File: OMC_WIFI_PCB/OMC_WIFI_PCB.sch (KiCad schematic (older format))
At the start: 27 parts, among them J1 SW, J10 Conn_01x02_Female_CanBus, J11 RJ14, J2 UART, J3 Screw_Terminal_01x02, J4 ICSP, J5 Conn_01x03_Female_SI, J6 Conn_01x02_Female_SV, J7 Conn_01x04_Female_SV, J8 Conn_01x03_Female_Rele, J9 Conn_01x07_Female_CanBus, SW1 SW_DIP_x06, U1 ATmega328P-MU, Y1 Crystal

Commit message: Actualización Esquemático
+ Módulo ZMPT101B
+ Módulo ACS712
+ ESP32 DevKitv1
+ Fuente de alimentación
+ Módulo Relay
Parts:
- removed C1: 0.1uf, SLAVE:CP_Radial_D5.0mm_P2.50mm, symbol Device:CP
- removed C2, C3: 22pF, SLAVE:C_0603_1608Metric_Pad1.05x0.95mm_HandSolder, symbol Device:C
- removed D1: LED, SLAVE:LED_D3.0mm, symbol Device:LED
- removed J1: SW, SLAVE:SolderWire-0.75sqmm_1x02_P4.8mm_D1.25mm_OD2.3mm, symbol Connector:Conn_01x02_Male
- removed J10: Conn_01x02_Female_CanBus, SLAVE:PinHeader_1x02_P2.54mm_Vertical, symbol Connector:Conn_01x02_Female
- removed J11: RJ14, SLAVE:RJ14_Connfly_DS1133-S4_Horizontal, symbol Connector:RJ13
- removed J2: UART, SLAVE:PinHeader_1x02_P2.54mm_Vertical, symbol Connector:Conn_01x02_Male
- removed J3: Screw_Terminal_01x02, SLAVE:TerminalBlock_bornier-2_P5.08mm, symbol Connector:Screw_Terminal_01x02
- removed J4: ICSP, SLAVE:PinHeader_2x03_P2.54mm_Vertical, symbol Connector_Generic:Conn_02x03_Odd_Even
- removed J6: Conn_01x02_Female_SV, SLAVE:SolderWire-0.75sqmm_1x02_P4.8mm_D1.25mm_OD2.3mm, symbol Connector:Conn_01x02_Female
- removed J7: Conn_01x04_Female_SV, SLAVE:PinHeader_1x04_P2.54mm_Vertical, symbol Connector:Conn_01x04_Female
- removed J8: Conn_01x03_Female_Rele, SLAVE:PinHeader_1x03_P2.54mm_Vertical, symbol Connector:Conn_01x03_Female
- removed J9: Conn_01x07_Female_CanBus, SLAVE:PinHeader_1x07_P2.54mm_Vertical, symbol Connector:Conn_01x07_Female
- removed PS1: HLK-PM01/5M05, SLAVE:Converter_ACDC_HiLink_HLK-PMxx, symbol Converter_ACDC:HLK-PM01
- removed R1, R3, R4, R5, R6, R7, R8: 10k, SLAVE:R_0603_1608Metric_Pad1.05x0.95mm_HandSolder, symbol Device:R
- removed R2: 330, SLAVE:R_0603_1608Metric_Pad1.05x0.95mm_HandSolder, symbol Device:R
- removed SW1: SW_DIP_x06, SLAVE:SW_DIP_SPSTx06_Piano_10.8x16.8mm_W7.62mm_P2.54mm, symbol Switch:SW_DIP_x06
- removed U1: ATmega328P-MU, SLAVE:TQFP-32_7x7mm_P0.8mm, symbol MCU_Microchip_ATmega:ATmega328P-MU
- removed Y1: Crystal, SLAVE:Crystal_SMD_HC49-SD, symbol Device:Crystal
- added J?: ESP32_Left, Connector_PinSocket_2.54mm:PinSocket_1x15_P2.54mm_Vertical, symbol Connector:Conn_01x15_Female
- added J?: ESP32_Right, Connector_PinSocket_2.54mm:PinSocket_1x15_P2.54mm_Vertical, symbol Connector:Conn_01x15_Female
- added J?: Conn_01x02_Female_SV, SLAVE:SolderWire-0.75sqmm_1x02_P4.8mm_D1.25mm_OD2.3mm, symbol Connector:Conn_01x02_Female
- added J?: Conn_01x02_Female, symbol Connector:Conn_01x02_Female
- added J?: Conn_01x04_Female, symbol Connector:Conn_01x04_Female
- added J?: Switch, Connector_PinHeader_2.54mm:PinHeader_1x02_P2.54mm_Vertical, symbol Connector:Conn_01x02_Male
- added J?: Conn_01x06_Female, symbol Connector:Conn_01x06_Female
- added J? (x2): Conn_01x03_Female, symbol Connector:Conn_01x03_Female
- added J?: Screw_Terminal_01x03, symbol Connector:Screw_Terminal_01x03
- added PS?: HLK-PM01, Converter_ACDC:Converter_ACDC_HiLink_HLK-PMxx, symbol Converter_ACDC:HLK-PM01
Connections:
- net labels added: 3V3, COM, CTS, D12, D13, D14, D15, D18, D19, D2, D21, D22, D23, D25, D26, D27_LED, D32_RELAY, D33, D34, D35, D4, D5, DTR, EN, I_ACS, NC, NO, RX0, RX2, TX0, TX2, VCC, VN_ACS, VP_ZMPT
- net labels removed: CS, H, INTERRUPT, I_Sensor, L, MISO, MOSI, RELAY, RESET, RX, SCK, TX, V_Sensor, XTAL1, XTAL2
- wire segments 144 -> 74
- no-connect marks 8 -> 1
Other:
- note added: "FT232R"
- note added: "Fuente de Alimentación HLK-PM01"
- note added: "Módulo ACS712 (Sensor Corriente)\n"
- note added: "Módulo ESP-WROOM32-DevKit1\n"
- note added: "Módulo Relay\n"
- note added: "Módulo ZMPT101B (Sensor Voltaje)\n"
- note removed: "Modulo CANBus con conector RJ11\n"
- note removed: "Modulo Relé\n"
- note removed: "Modulo Sensor Corriente\n"
- note removed: "Modulo Sensor Voltaje\n"
- note removed: "Programación ICSP\n"
- note removed: "Salida Serial\n"
- moved on the sheet: J5

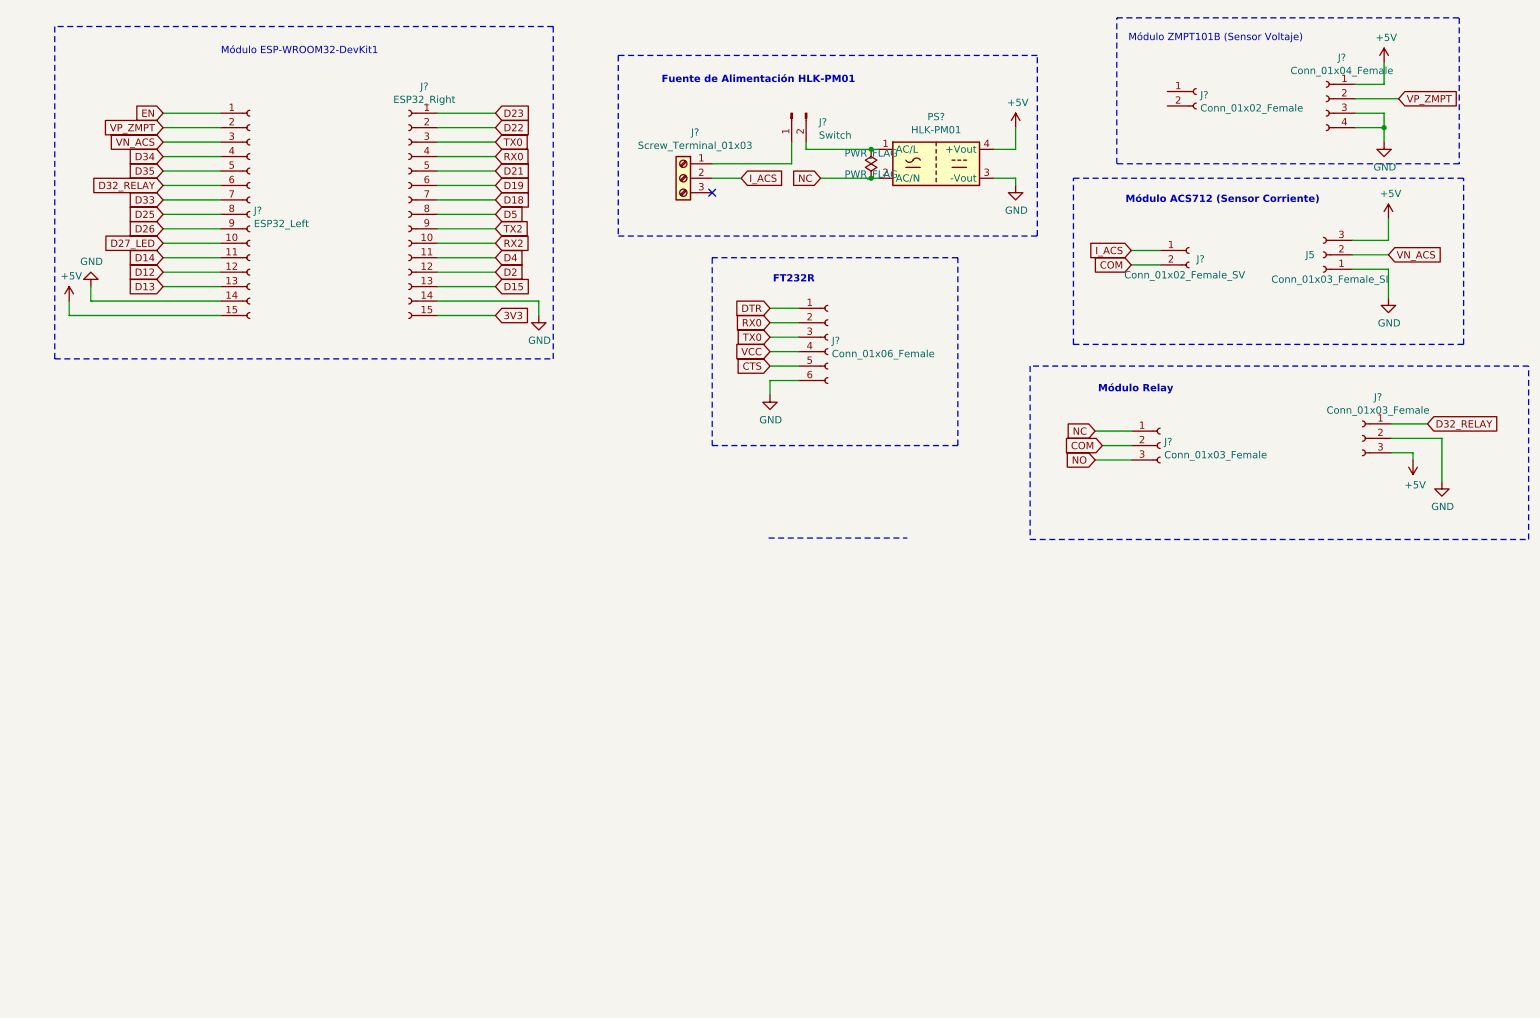
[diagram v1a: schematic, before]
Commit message: Actualización esquemático y PCB
+ Modificación del esquemático
+ Adición de footprints
+ Circuito amplificador para el relay
+ Modelo PCB del ZMPT101B
+ Adición de Librerías
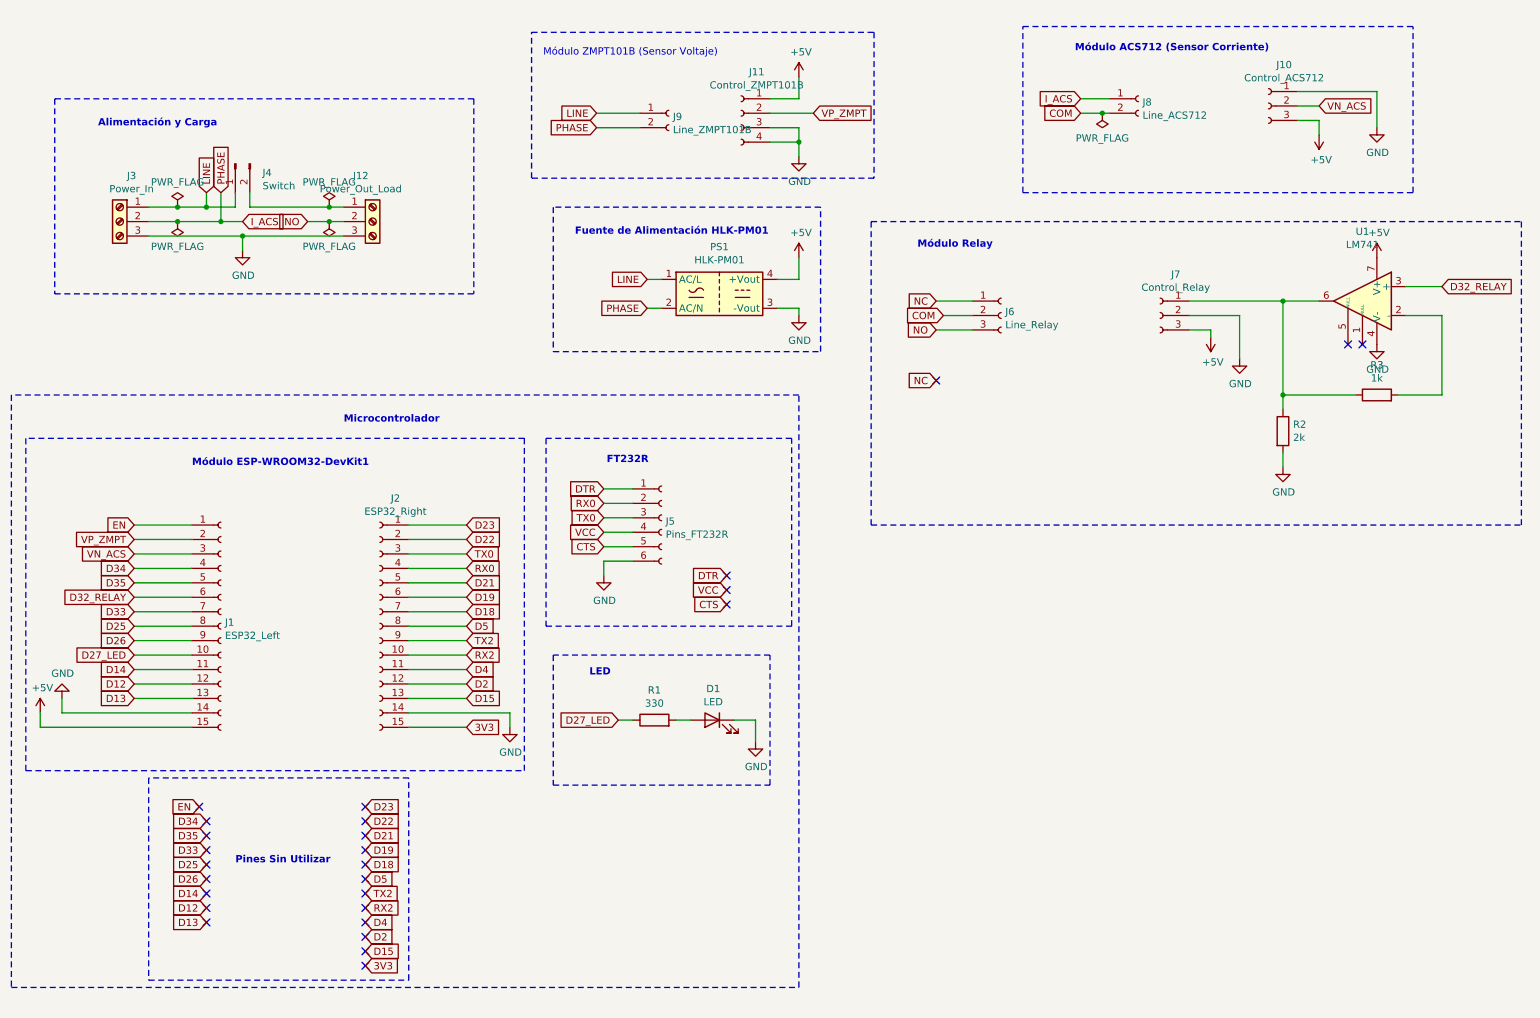
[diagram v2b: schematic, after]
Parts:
- removed J5: Conn_01x03_Female_SI, SLAVE:PinHeader_1x03_P2.54mm_Vertical, symbol Connector:Conn_01x03_Female
- removed J?: Conn_01x02_Female_SV, SLAVE:SolderWire-0.75sqmm_1x02_P4.8mm_D1.25mm_OD2.3mm, symbol Connector:Conn_01x02_Female
- added D1: LED, LED_THT:LED_D3.0mm, symbol Device:LED
- added J10: Control_ACS712, Connector_PinHeader_2.54mm:PinHeader_1x03_P2.54mm_Vertical, symbol Connector:Conn_01x03_Female
- added J12: Power_Out_Load, 6PCV-03-006:TE_5-1437652-4, symbol Connector:Screw_Terminal_01x03
- added J8: Line_ACS712, Connector_Wire:SolderWire-0.75sqmm_1x02_P4.8mm_D1.25mm_OD2.3mm, symbol Connector:Conn_01x02_Female
- added R1: 330, Resistor_SMD:R_2010_5025Metric_Pad1.40x2.65mm_HandSolder, symbol Device:R
- added R2: 2k, Resistor_SMD:R_1812_4532Metric_Pad1.30x3.40mm_HandSolder, symbol Device:R
- added R3: 1k, Resistor_SMD:R_2010_5025Metric_Pad1.40x2.65mm_HandSolder, symbol Device:R
- added U1: LM741, Package_DIP:DIP-8_W10.16mm, symbol Amplifier_Operational:LM741
- J11: renamed from J?; value Conn_01x04_Female -> Control_ZMPT101B; footprint (none) -> Connector_PinHeader_2.54mm:PinHeader_1x04_P2.54mm_Vertical
- J3: renamed from J?; value Screw_Terminal_01x03 -> Power_In; footprint (none) -> 6PCV-03-006:TE_5-1437652-4
- J4: renamed from J?; footprint Connector_PinHeader_2.54mm:PinHeader_1x02_P2.54mm_Vertical -> Connector_Wire:SolderWire-0.75sqmm_1x02_P7mm_D1.25mm_OD3.5mm
- J5: renamed from J?; value Conn_01x06_Female -> Pins_FT232R; footprint (none) -> Connector_PinSocket_2.54mm:PinSocket_1x06_P2.54mm_Vertical
- J6: renamed from J?; value Conn_01x03_Female -> Line_Relay; footprint (none) -> Connector_Wire:SolderWire-0.75sqmm_1x03_P4.8mm_D1.25mm_OD2.3mm
- J7: renamed from J?; value Conn_01x03_Female -> Control_Relay; footprint (none) -> Connector_Wire:SolderWire-0.75sqmm_1x03_P4.8mm_D1.25mm_OD2.3mm
- J9: renamed from J?; value Conn_01x02_Female -> Line_ZMPT101B; footprint (none) -> Connector_Wire:SolderWire-0.75sqmm_1x02_P4.8mm_D1.25mm_OD2.3mm
- gave numbers to parts that had none: 3
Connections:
- net +5V: now also J10.3 (Pin_3), U1.7 (V+)
- net COM: now also J8.2 (Pin_2)
- net D27_LED: now also R1.1
- net D32_RELAY: now also U1.3 (+); no longer J7.1 (Pin_1)
- net GND: now also J3.3 (Pin_3), D1.1 (K), J10.1 (Pin_1), J12.3 (Pin_3), R2.2, U1.4 (V-)
- net I_ACS: now also J9.2 (Pin_2), PS1.2 (AC/N), J8.1 (Pin_1)
- net NC: no longer PS1.2 (AC/N)
- net NO: now also J12.2 (Pin_2)
- net VN_ACS: now also J10.2 (Pin_2)
- net LINE: now reaches J9.1 (Pin_1)
- net LINE: now also J3.1 (Pin_1), J4.1 (Pin_1), PS1.1 (AC/L)
- net at J4.2 (Pin_2): now also J12.1 (Pin_1); no longer PS1.1 (AC/L)
- new net: D1.2 (A), R1.2
- new net: R3.2, U1.2 (-)
- new net: J7.1 (Pin_1), R2.1, R3.1, U1.6
- no-connect marks 1 -> 27
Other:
- note added: "Alimentación y Carga"
- note added: "LED"
- note added: "Microcontrolador"
- note added: "Pines Sin Utilizar"
- moved on the sheet: J1, J11, J2, J3, J4, J5, J6, J7, J9, PS1
